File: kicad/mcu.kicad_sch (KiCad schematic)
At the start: 16 parts, among them IC2 STM32C552CET6, J11 Conn_01x02, J2 Conn_ARM_SWD_TagConnect_TC2030, J4 Conn_01x02, Y2 830069528, Y4 32.768kHz

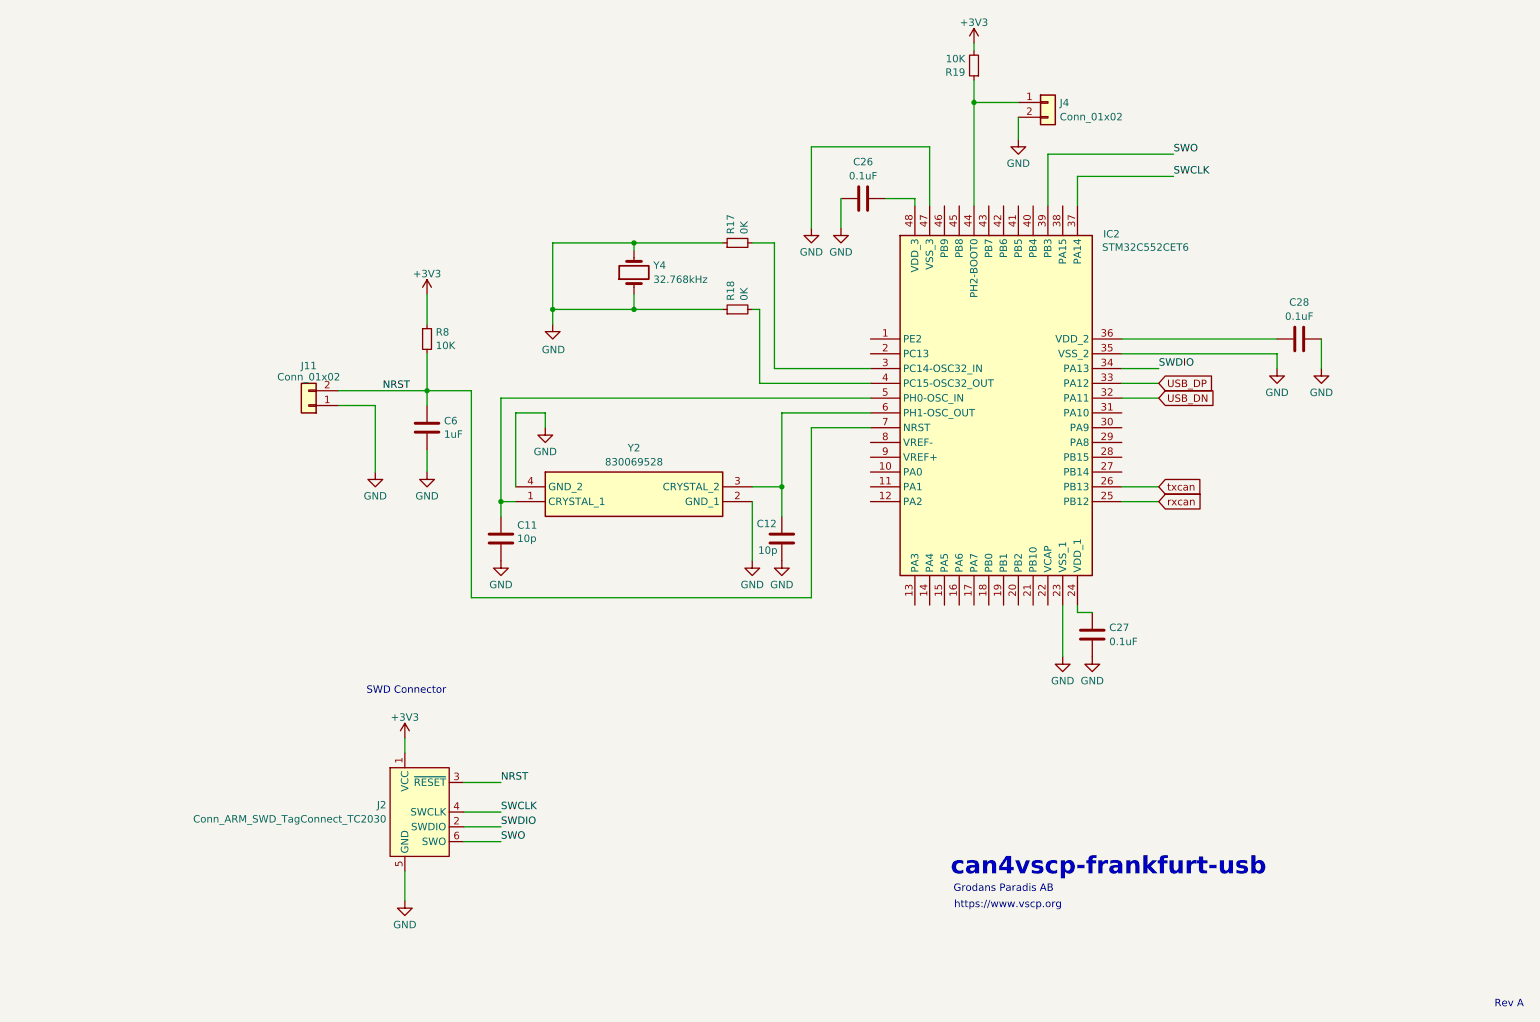
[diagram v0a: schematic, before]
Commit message: Changed crystal to TXC 7V series
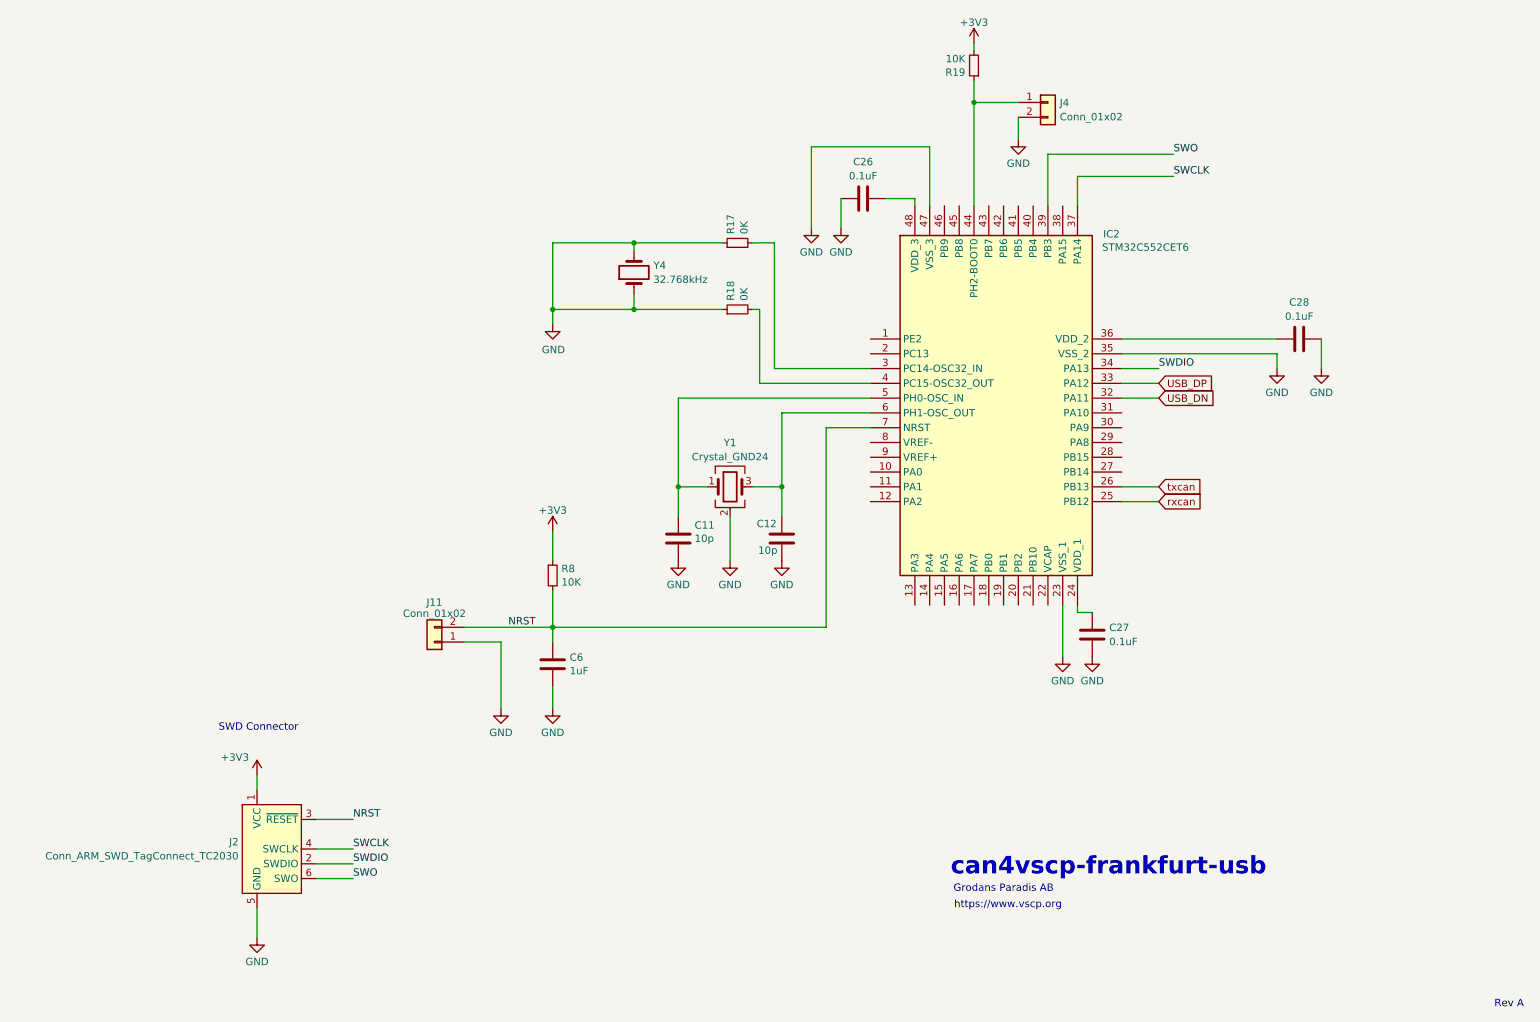
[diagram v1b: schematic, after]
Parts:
- removed Y2: 830069528, 830069528, symbol TCAN3404:830069528
- added Y1: Crystal_GND24, Crystal:Crystal_SMD_TXC_7M-4Pin_3.2x2.5mm_HandSoldering, symbol Device:Crystal_GND24
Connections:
- net GND: now also Y1.2 (G), Y1.4 (G)
- net at C11.1, IC2.5 (PH0-OSC_IN): now also Y1.1
- net at C12.1, IC2.6 (PH1-OSC_OUT): now also Y1.3
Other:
- moved on the sheet: C11, C6, J11, J2, R8

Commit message: Fixed power issue
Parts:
- removed J2: Conn_ARM_SWD_TagConnect_TC2030, Connector:Tag-Connect_TC2030-IDC-FP_2x03_P1.27mm_Vertical, symbol Connector:Conn_ARM_SWD_TagConnect_TC2030
- added J7: Conn_ARM_JTAG_SWD_10, symbol Connector:Conn_ARM_JTAG_SWD_10
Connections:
- net +3V3: now also C26.2, C27.2, C28.1, IC2.24 (VDD_1), IC2.36 (VDD_2), IC2.48 (VDD_3), J7.1 (VTref)
- net GND: now also J7.3 (GND), J7.5 (GND), J7.9 (GNDDetect)
- net NRST: now also J7.10 (~{RESET})
- net SWCLK: now also J7.4 (SWCLK/TCK)
- net SWDIO: now also J7.2 (SWDIO/TMS)
- net SWO: now also J7.6 (SWO/TDO)
- no-connect marks 0 -> 1
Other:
- note added: "Default is on Remove to run system bootloader (USART, USB, FDCAN, SPI) on startup"
- note removed: "Rev A"
- moved on the sheet: C26

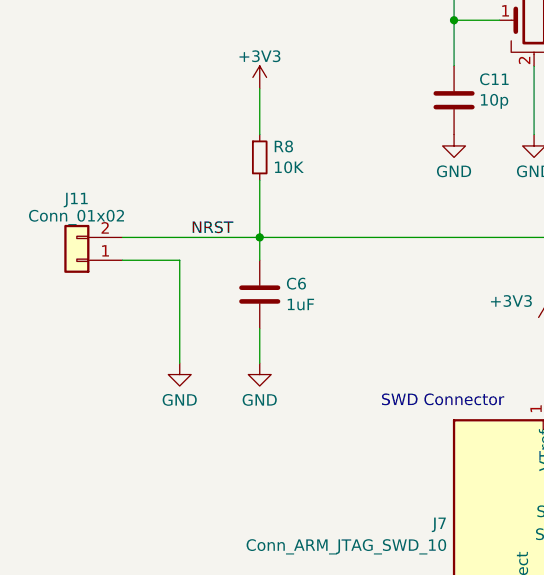
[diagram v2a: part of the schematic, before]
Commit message: Added butons
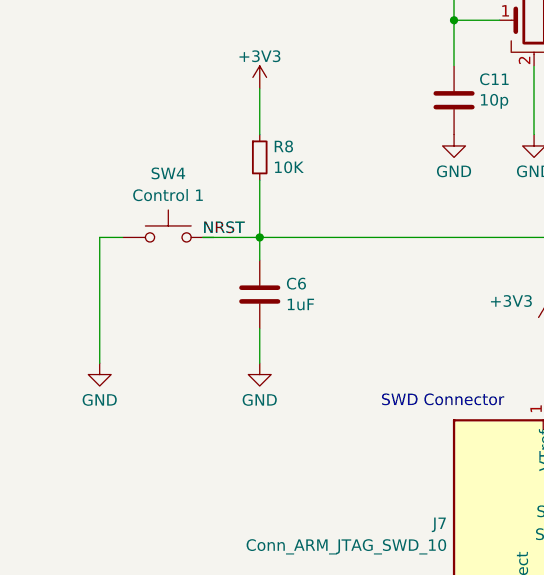
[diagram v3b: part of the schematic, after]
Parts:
- removed J11: Conn_01x02, Connector_PinHeader_2.54mm:PinHeader_1x02_P2.54mm_Vertical, symbol Connector_Generic:Conn_01x02
- added SW4: Control 1, Button_Switch_SMD:SW_SPST_Omron_B3FS-100xP, symbol Switch:SW_Omron_B3FS
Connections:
- net GND: now also SW4.1
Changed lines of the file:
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@@
-	(wire
-		(pts
-			(xy 96.52 128.27) (xy 111.76 128.27)
-		)
-		(stroke
-			(width 0)
-			(type default)
-		)
-	)
 	(wire
 		(pts
@@
 	(wire
 		(pts
-			(xy 96.52 130.81) (xy 102.87 130.81)
-		)
-		(stroke
-			(width 0)
-			(type default)
-		)
-	)
-	(wire
-		(pts
 			(xy 209.55 106.68) (xy 215.9 106.68)
 		)
@@
 	(wire
 		(pts
-			(xy 102.87 130.81) (xy 102.87 142.24)
-		)
-		(stroke
-			(width 0)
-			(type default)
-		)
-	)
-	(wire
-		(pts
 			(xy 147.32 73.66) (xy 146.05 73.66)
 		)
@@
 	(wire
 		(pts
+			(xy 93.98 128.27) (xy 93.98 142.24)
+		)
+		(stroke
+			(width 0)
+			(type default)
+		)
+	)
+	(wire
+		(pts
 			(xy 209.55 81.28) (xy 236.22 81.28)
 		)
@@
 	(wire
 		(pts
+			(xy 96.52 128.27) (xy 93.98 128.27)
+		)
+		(stroke
+			(width 0)
+			(type default)
+		)
+	)
+	(wire
+		(pts
 			(xy 209.55 86.36) (xy 215.9 86.36)
 		)
@@
 		(pts
 			(xy 125.73 73.66) (xy 140.97 73.66)
+		)
+		(stroke
+			(width 0)
+			(type default)
+		)
+	)
+	(wire
+		(pts
+			(xy 105.41 128.27) (xy 111.76 128.27)
 		)
 		(stroke
@@
 	)
 	(label "NRST"
-		(at 104.14 128.27 0)
+		(at 105.41 128.27 0)
 		(effects
 			(font
@@
 	)
 	(symbol
+		(lib_id "Switch:SW_Omron_B3FS")
+		(at 101.6 128.27 0)
+		(unit 1)
+		(body_style 1)
+		(exclude_from_sim no)
+		(in_bom yes)
+		(on_board yes)
+		(in_pos_files yes)
+		(dnp no)
+		(fields_autoplaced yes)
+		(property "Reference" "SW4"
+			(at 101.6 121.2045 0)
+			(show_name no)
+			(do_not_autoplace no)
+			(effects
+				(font
+					(size 1.27 1.27)
+				)
+			)
+		)
+		(property "Value" "Control 1"
+			(at 101.6 123.6288 0)
+			(show_name no)
+			(do_not_autoplace no)
+			(effects
+				(font
+					(size 1.27 1.27)
+				)
+			)
+		)
+		(property "Footprint" "Button_Switch_SMD:SW_SPST_Omron_B3FS-100xP"
+			(at 101.6 123.19 0)
+			(hide yes)
+			(show_name no)
+			(do_not_autoplace no)
+			(effects
+				(font
+					(size 1.27 1.27)
+				)
+			)
+		)
+		(property "Datasheet" "https://omronfs.omron.com/en_US/ecb/products/pdf/en-b3fs.pdf"
+			(at 101.6 123.19 0)
+			(hide yes)
+			(show_name no)
+			(do_not_autoplace no)
+			(effects
+				(font
+					(size 1.27 1.27)
+				)
+			)
+		)
+		(property "Description" "Omron B3FS 6x6mm single pole normally-open tactile switch"
+			(at 101.6 128.27 0)
+			(hide yes)
+			(show_name no)
+			(do_not_autoplace no)
+			(effects
+				(font
+					(size 1.27 1.27)
+				)
+			)
+		)
+		(pin "2"
+		)
+		(pin "1"
+		)
+		(instances
+			(project "vscp-din-stm32h552-can-z102"
+				(path "/a1545928-1195-40b9-b3c4-78f837012afb/a2c85583-6e76-4726-8b5c-5d610fd6c58c"
+					(reference "SW4")
+					(unit 1)
+				)
+			)
+		)
+	)
+	(symbol
 		(lib_id "Device:C")
 		(at 151.13 113.03 0)
@@
 				(path "/a1545928-1195-40b9-b3c4-78f837012afb/a2c85583-6e76-4726-8b5c-5d610fd6c58c"
 					(reference "C12")
-					(unit 1)
-				)
-			)
-		)
-	)
-	(symbol
-		(lib_id "power:GND")
-		(at 102.87 142.24 0)
-		(unit 1)
-		(body_style 1)
-		(exclude_from_sim no)
-		(in_bom yes)
-		(on_board yes)
-		(in_pos_files yes)
-		(dnp no)
-		(fields_autoplaced yes)
-		(property "Reference" "#PWR01"
-			(at 102.87 148.59 0)
-			(hide yes)
-			(show_name no)
-			(do_not_autoplace no)
-			(effects
-				(font
-					(size 1.27 1.27)
-				)
-			)
-		)
-		(property "Value" "GND"
-			(at 102.87 146.3731 0)
-			(show_name no)
-			(do_not_autoplace no)
-			(effects
-				(font
-					(size 1.27 1.27)
-				)
-			)
-		)
-		(property "Footprint" ""
-			(at 102.87 142.24 0)
-			(hide yes)
-			(show_name no)
-			(do_not_autoplace no)
-			(effects
-				(font
-					(size 1.27 1.27)
-				)
-			)
-		)
-		(property "Datasheet" ""
-			(at 102.87 142.24 0)
-			(hide yes)
-			(show_name no)
-			(do_not_autoplace no)
-			(effects
-				(font
-					(size 1.27 1.27)
-				)
-			)
-		)
-		(property "Description" "Power symbol creates a global label with name \"GND\" , ground"
-			(at 102.87 142.24 0)
-			(hide yes)
-			(show_name no)
-			(do_not_autoplace no)
-			(effects
-				(font
-					(size 1.27 1.27)
-				)
-			)
-		)
-		(pin "1"
-		)
-		(instances
-			(project "vscp-din-stm32h552-can-z102"
-				(path "/a1545928-1195-40b9-b3c4-78f837012afb/a2c85583-6e76-4726-8b5c-5d610fd6c58c"
-					(reference "#PWR01")
 					(unit 1)
 				)
@@
 	(symbol
 		(lib_id "power:GND")
+		(at 93.98 142.24 0)
+		(unit 1)
+		(body_style 1)
+		(exclude_from_sim no)
+		(in_bom yes)
+		(on_board yes)
+		(in_pos_files yes)
+		(dnp no)
+		(fields_autoplaced yes)
+		(property "Reference" "#PWR035"
+			(at 93.98 148.59 0)
+			(hide yes)
+			(show_name no)
+			(do_not_autoplace no)
+			(effects
+				(font
+					(size 1.27 1.27)
+				)
+			)
+		)
+		(property "Value" "GND"
+			(at 93.98 146.3731 0)
+			(show_name no)
+			(do_not_autoplace no)
+			(effects
+				(font
+					(size 1.27 1.27)
+				)
+			)
+		)
+		(property "Footprint" ""
+			(at 93.98 142.24 0)
+			(hide yes)
+			(show_name no)
+			(do_not_autoplace no)
+			(effects
+				(font
+					(size 1.27 1.27)
+				)
+			)
+		)
+		(property "Datasheet" ""
+			(at 93.98 142.24 0)
+			(hide yes)
+			(show_name no)
+			(do_not_autoplace no)
+			(effects
+				(font
+					(size 1.27 1.27)
+				)
+			)
+		)
+		(property "Description" "Power symbol creates a global label with name \"GND\" , ground"
+			(at 93.98 142.24 0)
+			(hide yes)
+			(show_name no)
+			(do_not_autoplace no)
+			(effects
+				(font
+					(size 1.27 1.27)
+				)
+			)
+		)
+		(pin "1"
+		)
+		(instances
+			(project "vscp-din-stm32h552-can-z102"
+				(path "/a1545928-1195-40b9-b3c4-78f837012afb/a2c85583-6e76-4726-8b5c-5d610fd6c58c"
+					(reference "#PWR035")
+					(unit 1)
+				)
+			)
+		)
+	)
+	(symbol
+		(lib_id "power:GND")
 		(at 111.76 142.24 0)
 		(unit 1)
@@
 					(unit 1)
 				)
-			)
-		)
-	)
-	(symbol
-		(lib_id "Connector_Generic:Conn_01x02")
-		(at 91.44 130.81 180)
-		(unit 1)
-		(body_style 1)
-		(exclude_from_sim no)
-		(in_bom yes)
-		(on_board yes)
-		(in_pos_files yes)
-		(dnp no)
-		(fields_autoplaced yes)
-		(property "Reference" "J11"
-			(at 91.44 123.9901 0)
-			(show_name no)
-			(do_not_autoplace no)
-			(effects
-				(font
-					(size 1.27 1.27)
-				)
-			)
-		)
-		(property "Value" "Conn_01x02"
-			(at 91.44 125.9111 0)
-			(show_name no)
-			(do_not_autoplace no)
-			(effects
-				(font
-					(size 1.27 1.27)
-				)
-			)
-		)
-		(property "Footprint" "Connector_PinHeader_2.54mm:PinHeader_1x02_P2.54mm_Vertical"
-			(at 91.44 130.81 0)
-			(hide yes)
-			(show_name no)
-			(do_not_autoplace no)
-			(effects
-				(font
-					(size 1.27 1.27)
-				)
-			)
-		)
-		(property "Datasheet" ""
-			(at 91.44 130.81 0)
-			(hide yes)
-			(show_name no)
-			(do_not_autoplace no)
-			(effects
-				(font
-					(size 1.27 1.27)
-				)
-			)
-		)
-		(property "Description" "Generic connector, single row, 01x02, script generated (kicad-library-utils/schlib/autogen/connector/)"
-			(at 91.44 130.81 0)
-			(hide yes)
-			(show_name no)
-			(do_not_autoplace no)
-			(effects
-				(font
-					(size 1.27 1.27)
-				)
-			)
-		)
-		(pin "1"
-		)
-		(pin "2"
-		)
-		(instances
-			(project "vscp-din-stm32h552-can-z102"
-				(path "/a1545928-1195-40b9-b3c4-78f837012afb/a2c85583-6e76-4726-8b5c-5d610fd6c58c"
-					(reference "J11")
-					(unit 1)
-				)

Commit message: Reversion A schema and PCB
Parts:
- IC1: renamed from IC2; footprint QFP50P900X900X160-48N -> STM32C552CET6:QFP50P900X900X160-48N
- J4: footprint (none) -> Connector_PinHeader_2.54mm:PinHeader_1x02_P2.54mm_Vertical
- J7: footprint (none) -> Connector_PinHeader_1.27mm:PinHeader_2x05_P1.27mm_Vertical
- SW4: value Control 1 -> RESET
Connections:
- net NRST: now also SW4.2
- net BOOT0: now reaches IC1.44 (PH2-BOOT0), J4.1 (Pin_1), R19.1
- net +3V3 renamed +3.3V
- no-connect marks 1 -> 31
